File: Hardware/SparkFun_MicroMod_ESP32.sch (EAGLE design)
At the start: 45 parts, among them J1 MICROMOD-2222, Q2 MBT3904DW1T1, U1 W25QXX128MBIT-6X5, U2 ESP3212, U4 CP2102N, Y1 40MHZ, Y2 32.768kHz

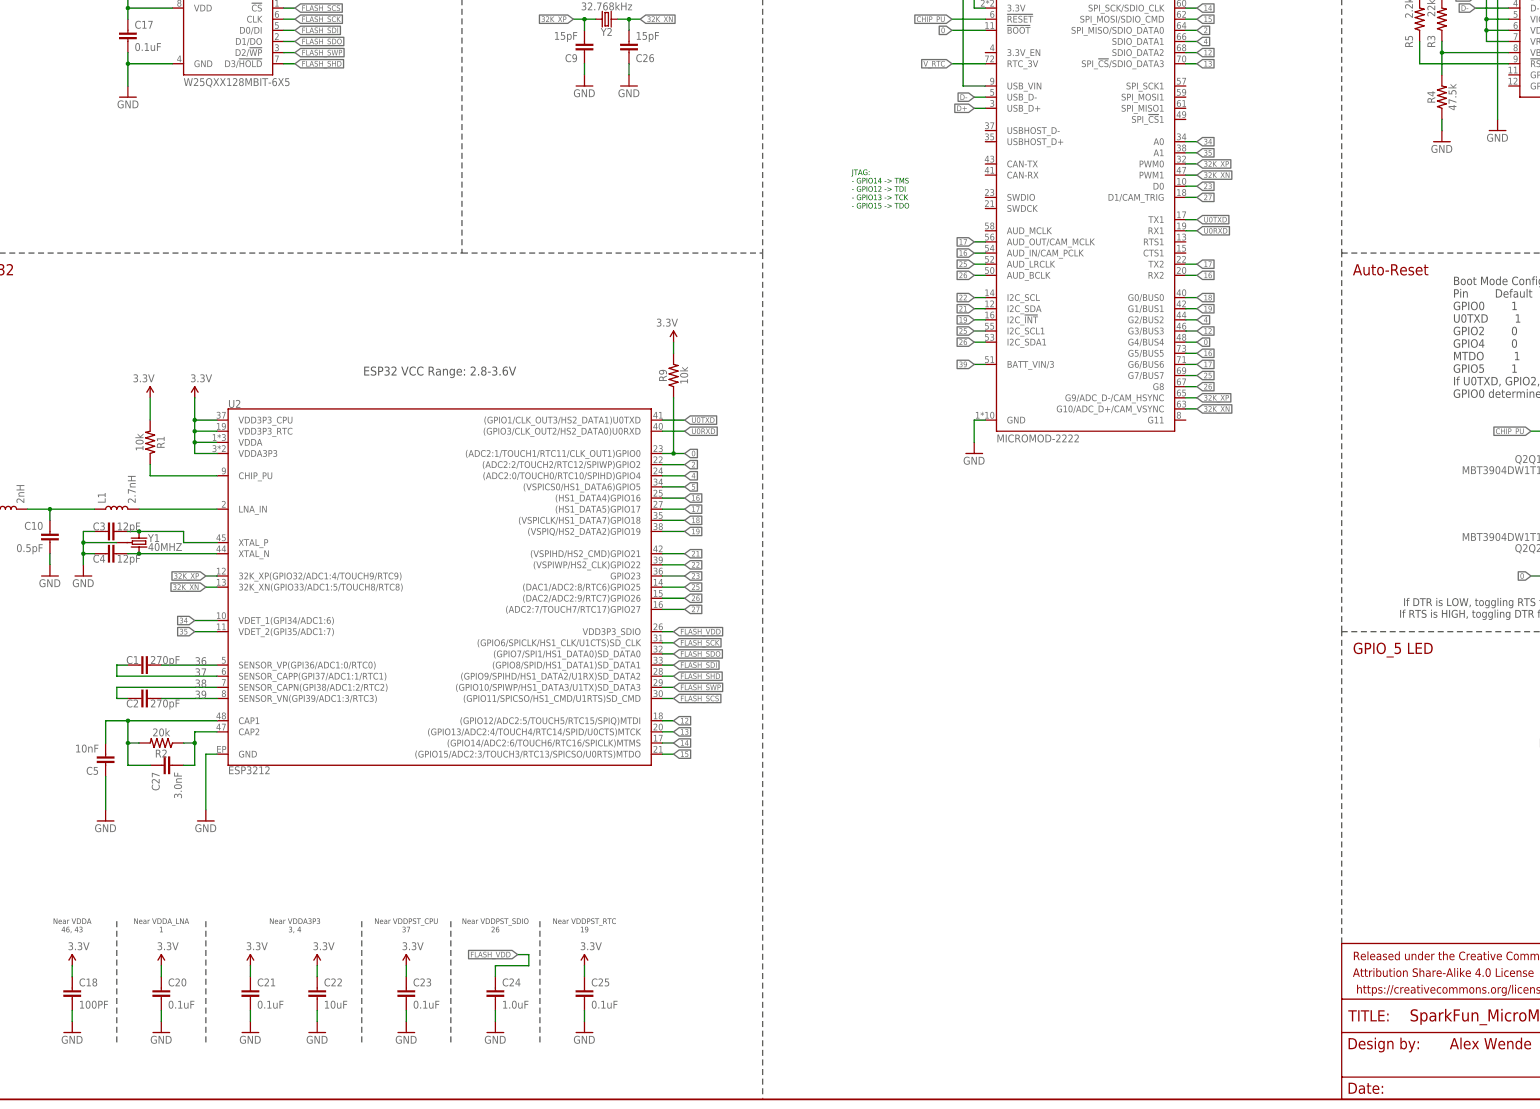
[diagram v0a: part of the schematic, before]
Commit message: updated Prod_IDs
Added missing PROD_IDs
Added Logos to sch
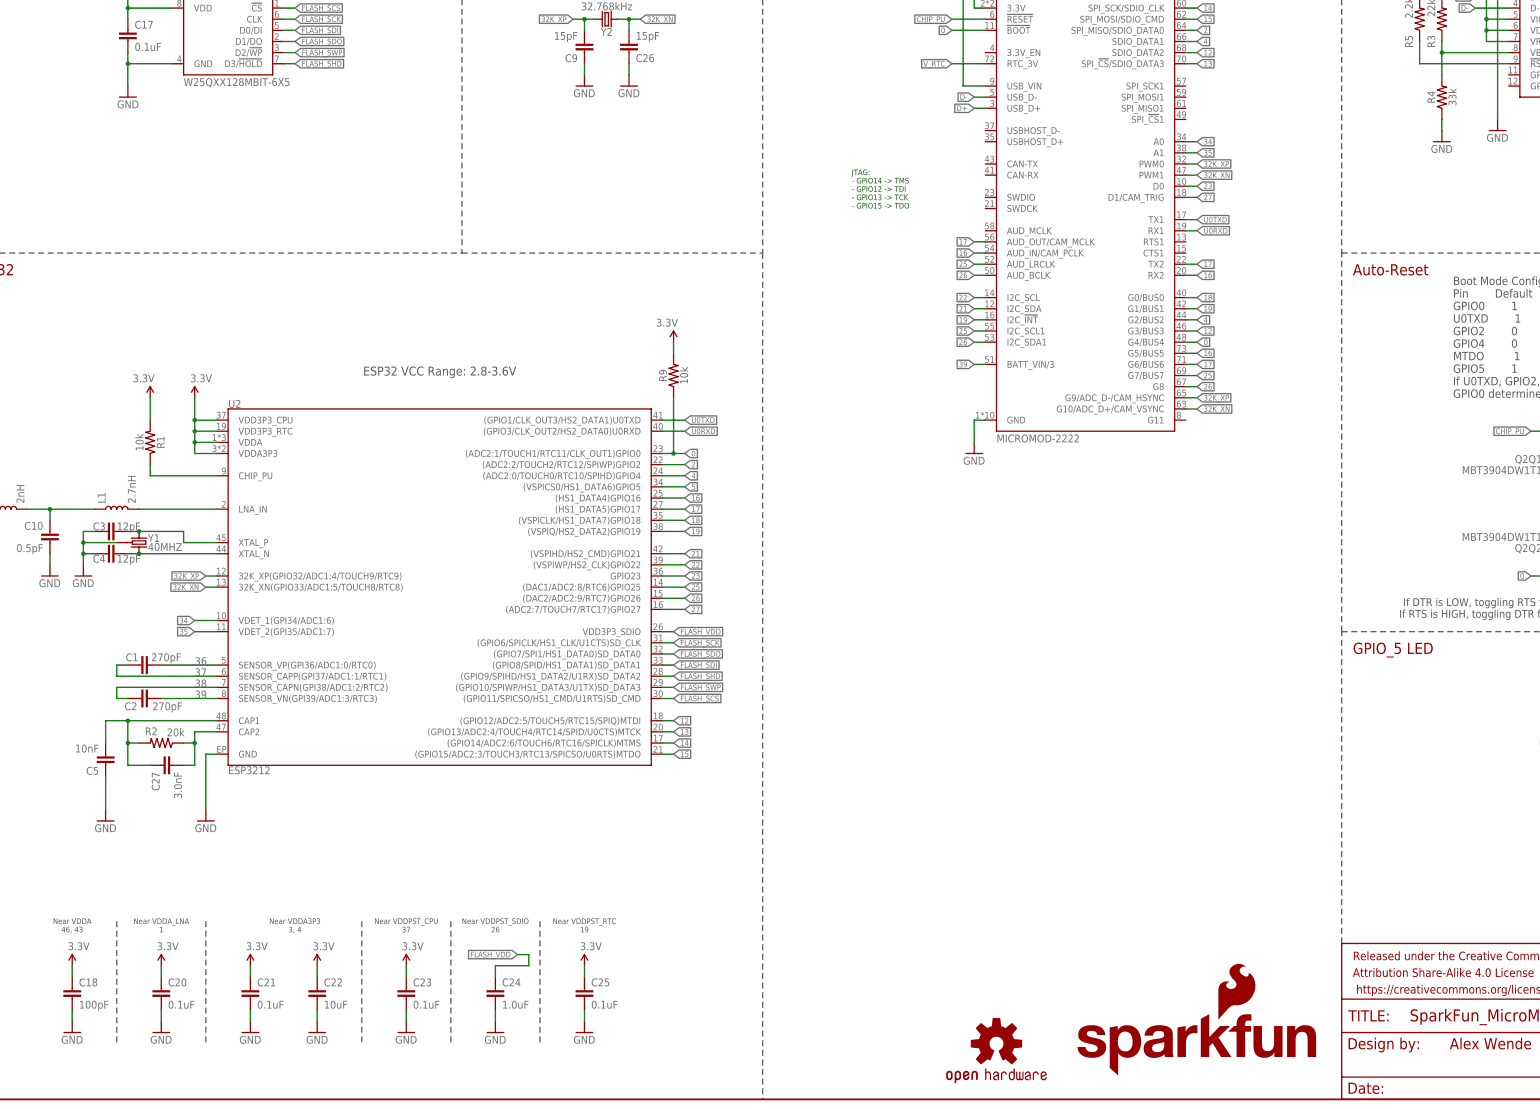
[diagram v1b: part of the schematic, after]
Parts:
- added LOGO2: SFE_LOGO_NAME_FLAME.1_INCH, SparkFun-Aesthetics:SFE_LOGO_NAME_FLAME.1_INCH
- added LOGO3: OSHW-LOGOS, SparkFun-Aesthetics:OSHW-LOGOS
- C1, C2: device SparkFun-Capacitors:4.7UF-0402_TIGHT-6.3V-20%-X5R -> SparkFun-Capacitors:270PF-0402T-50V-5%
- C10: device SparkFun-Capacitors:0.5PF-0402_TIGHT-20V-PM0.05PF-NP0 -> SparkFun-Capacitors:0.5PF-0402_TIGHT-50V-PM0.05PF-NP0
- C18: value 100PF -> 100pF; device SparkFun-Capacitors:CAP-0402-TIGHT -> SparkFun-Capacitors:100PF-0402T-50V-5%
- C27: device SparkFun-Capacitors:4.7UF-0402_TIGHT-6.3V-20%-X5R -> SparkFun-Capacitors:3.0NF-0402T-50V-5%
- R2: device SparkFun-Resistors:5.1KOHM-0402T-1/16W-1% -> SparkFun-Resistors:20KOHM-0402T-1/16W-1%
- R4: value 47.5k -> 33k; device SparkFun-Resistors:5.1KOHM-0402T-1/16W-1% -> SparkFun-Resistors:33KOHM-0402T-1/16W-1%
- Y1: device SparkFun-Clocks:CRYSTAL-40MHZ-SMD2-2X2.5MM -> SparkFun-Clocks:CRYSTAL-40MHZ-SMD-2X2.5MM
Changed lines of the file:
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@@
 <?xml version="1.0" encoding="utf-8"?>
 <!DOCTYPE eagle SYSTEM "eagle.dtd">
-<eagle version="9.6.0">
+<eagle version="9.4.1">
 <drawing>
 <settings>
-<setting alwaysvectorfont="yes"/>
+<setting alwaysvectorfont="no"/>
 <setting keepoldvectorfont="yes"/>
 <setting verticaltext="up"/>
@@
 <part name="SUPPLY2" library="SparkFun-Aesthetics" deviceset="3.3V" device=""/>
 <part name="GND2" library="SparkFun-Aesthetics" deviceset="GND" device=""/>
-<part name="Y1" library="SparkFun-Clocks" deviceset="CRYSTAL-40MHZ" device="-SMD2-2X2.5MM" value="40MHZ"/>
+<part name="Y1" library="SparkFun-Clocks" deviceset="CRYSTAL-40MHZ" device="-SMD-2X2.5MM" value="40MHZ"/>
 <part name="C3" library="SparkFun-Capacitors" deviceset="12PF" device="-0402T-50V-5%" value="12pF"/>
 <part name="C4" library="SparkFun-Capacitors" deviceset="12PF" device="-0402T-50V-5%" value="12pF"/>
-<part name="C1" library="SparkFun-Capacitors" deviceset="4.7UF" device="-0402_TIGHT-6.3V-20%-X5R" value="270pF"/>
-<part name="C2" library="SparkFun-Capacitors" deviceset="4.7UF" device="-0402_TIGHT-6.3V-20%-X5R" value="270pF"/>
+<part name="C1" library="SparkFun-Capacitors" deviceset="270PF" device="-0402T-50V-5%" value="270pF"/>
+<part name="C2" library="SparkFun-Capacitors" deviceset="270PF" device="-0402T-50V-5%" value="270pF"/>
 <part name="C5" library="SparkFun-Capacitors" deviceset="10NF" device="-0402T-25V-10%" value="10nF"/>
-<part name="R2" library="SparkFun-Resistors" deviceset="5.1KOHM" device="-0402T-1/16W-1%" value="20k"/>
+<part name="R2" library="SparkFun-Resistors" deviceset="20KOHM" device="-0402T-1/16W-1%" value="20k"/>
 <part name="GND3" library="SparkFun-Aesthetics" deviceset="GND" device=""/>
 <part name="GND36" library="SparkFun-Aesthetics" deviceset="GND" device=""/>
@@
 <part name="R17" library="SparkFun-Resistors" deviceset="10KOHM" device="-0402T-1/16W-1%" value="10k"/>
 <part name="R18" library="SparkFun-Resistors" deviceset="10KOHM" device="-0402T-1/16W-1%" value="10k"/>
-<part name="C18" library="SparkFun-Capacitors" deviceset="CAP" device="-0402-TIGHT" value="100PF"/>
+<part name="C18" library="SparkFun-Capacitors" deviceset="100PF" device="-0402T-50V-5%" value="100pF"/>
 <part name="SUPPLY9" library="SparkFun-Aesthetics" deviceset="3.3V" device=""/>
 <part name="GND5" library="SparkFun-Aesthetics" deviceset="GND" device=""/>
@@
 <part name="SUPPLY17" library="SparkFun-Aesthetics" deviceset="3.3V" device=""/>
 <part name="U2" library="esp32-thing-temp" deviceset="ESP3212" device=""/>
-<part name="C27" library="SparkFun-Capacitors" deviceset="4.7UF" device="-0402_TIGHT-6.3V-20%-X5R" value="3.0nF"/>
+<part name="C27" library="SparkFun-Capacitors" deviceset="3.0NF" device="-0402T-50V-5%" value="3.0nF"/>
 <part name="GND40" library="SparkFun-Aesthetics" deviceset="GND" device=""/>
 <part name="U4" library="SparkFun-IC-Comms" deviceset="CP2102N" device=""/>
@@
 <part name="SUPPLY8" library="SparkFun-Aesthetics" deviceset="3.3V" device=""/>
 <part name="R3" library="SparkFun-Resistors" deviceset="22KOHM" device="-0402_TIGHT-1/10W-1%" value="22k"/>
-<part name="R4" library="SparkFun-Resistors" deviceset="5.1KOHM" device="-0402T-1/16W-1%" value="47.5k"/>
+<part name="R4" library="SparkFun-Resistors" deviceset="33KOHM" device="-0402T-1/16W-1%" value="33k"/>
 <part name="GND11" library="SparkFun-Aesthetics" deviceset="GND" device=""/>
 <part name="SUPPLY14" library="SparkFun-Aesthetics" deviceset="V_USB" device=""/>
@@
 <part name="L1" library="SparkFun-Coils" deviceset="INDUCTOR" device="-0402_TIGHT-2.7NH" value="2.7nH"/>
 <part name="L2" library="SparkFun-Coils" deviceset="INDUCTOR" device="-0402_TIGHT-2.0NH" value="2nH"/>
-<part name="C10" library="SparkFun-Capacitors" deviceset="0.5PF" device="-0402_TIGHT-20V-PM0.05PF-NP0" value="0.5pF"/>
+<part name="C10" library="SparkFun-Capacitors" deviceset="0.5PF" device="-0402_TIGHT-50V-PM0.05PF-NP0" value="0.5pF"/>
 <part name="GND12" library="SparkFun-Aesthetics" deviceset="GND" device=""/>
 <part name="FD1" library="SparkFun-Aesthetics" deviceset="FIDUCIAL" device="UFIDUCIAL" value="FIDUCIALUFIDUCIAL"/>
@@
 <part name="FD4" library="SparkFun-Aesthetics" deviceset="FIDUCIAL" device="UFIDUCIAL" value="FIDUCIALUFIDUCIAL"/>
 <part name="LOGO1" library="SparkFun-Aesthetics" deviceset="SPECIAL_INSTRUCTIONS" device="-ORDERING"/>
+<part name="LOGO2" library="SparkFun-Aesthetics" deviceset="SFE_LOGO_NAME_FLAME" device=".1_INCH"/>
+<part name="LOGO3" library="SparkFun-Aesthetics" deviceset="OSHW-LOGO" device="S"/>
 </parts>
 <sheets>
@@
 </instance>
 <instance part="C1" gate="G$1" x="58.42" y="99.06" smashed="yes" rot="R90">
-<attribute name="NAME" x="55.88" y="99.314" size="1.778" layer="95" rot="MR0"/>
-<attribute name="VALUE" x="58.42" y="99.314" size="1.778" layer="96"/>
+<attribute name="NAME" x="52.832" y="99.949" size="1.778" layer="95" font="vector"/>
+<attribute name="VALUE" x="58.674" y="99.949" size="1.778" layer="96" font="vector"/>
 </instance>
 <instance part="C2" gate="G$1" x="58.42" y="91.44" smashed="yes" rot="MR270">
-<attribute name="NAME" x="55.88" y="91.186" size="1.778" layer="95" align="top-right"/>
-<attribute name="VALUE" x="58.42" y="91.186" size="1.778" layer="96" rot="MR180"/>
+<attribute name="NAME" x="52.578" y="90.551" size="1.778" layer="95" font="vector" rot="MR180"/>
+<attribute name="VALUE" x="58.928" y="90.551" size="1.778" layer="96" font="vector" rot="MR180"/>
 </instance>
 <instance part="C5" gate="G$1" x="48.26" y="78.74" smashed="yes" rot="R180">
@@
 <attribute name="VALUE" x="46.736" y="80.899" size="1.778" layer="96" font="vector" rot="R180"/>
 </instance>
-<instance part="R2" gate="R1" x="60.96" y="81.28" smashed="yes" rot="R180">
-<attribute name="NAME" x="60.96" y="79.756" size="1.778" layer="95" font="vector" rot="R180" align="bottom-center"/>
-<attribute name="VALUE" x="60.96" y="82.804" size="1.778" layer="96" font="vector" rot="R180" align="top-center"/>
+<instance part="R2" gate="G$1" x="60.96" y="81.28" smashed="yes" rot="R180">
+<attribute name="NAME" x="58.674" y="83.058" size="1.778" layer="95" font="vector" align="bottom-center"/>
+<attribute name="VALUE" x="64.262" y="82.804" size="1.778" layer="96" font="vector" rot="R180" align="top-center"/>
 </instance>
 <instance part="GND3" gate="1" x="48.26" y="63.5" smashed="yes">
@@
 <attribute name="VALUE" x="351.536" y="248.92" size="1.778" layer="96" font="vector" rot="R270" align="top-center"/>
 </instance>
-<instance part="R4" gate="R1" x="353.06" y="228.6" smashed="yes" rot="R90">
+<instance part="R4" gate="G$1" x="353.06" y="228.6" smashed="yes" rot="R90">
 <attribute name="NAME" x="351.536" y="228.6" size="1.778" layer="95" font="vector" rot="R90" align="bottom-center"/>
 <attribute name="VALUE" x="354.584" y="228.6" size="1.778" layer="96" font="vector" rot="R90" align="top-center"/>
@@
 <instance part="FD4" gate="G$1" x="424.18" y="17.78" smashed="yes"/>
 <instance part="LOGO1" gate="G$1" x="408.94" y="33.02" smashed="yes"/>
+<instance part="LOGO2" gate="G$1" x="269.24" y="5.08" smashed="yes"/>
+<instance part="LOGO3" gate="G$1" x="251.46" y="12.7" smashed="yes"/>
 </instances>
 <busses>
@@
 </segment>
 <segment>
-<pinref part="R4" gate="R1" pin="1"/>
+<pinref part="R4" gate="G$1" pin="1"/>
 <wire x1="353.06" y1="223.52" x2="353.06" y2="220.98" width="0.1524" layer="91"/>
 <pinref part="GND11" gate="1" pin="GND"/>
@@
 <wire x1="53.34" y1="76.2" x2="53.34" y2="81.28" width="0.1524" layer="91"/>
 <junction x="53.34" y="86.36"/>
-<pinref part="R2" gate="R1" pin="2"/>
+<pinref part="R2" gate="G$1" pin="2"/>
 <wire x1="53.34" y1="81.28" x2="53.34" y2="86.36" width="0.1524" layer="91"/>
 <wire x1="55.88" y1="81.28" x2="53.34" y2="81.28" width="0.1524" layer="91"/>
@@
 <wire x1="68.58" y1="81.28" x2="68.58" y2="83.82" width="0.1524" layer="91"/>
 <wire x1="68.58" y1="83.82" x2="73.66" y2="83.82" width="0.1524" layer="91"/>
-<pinref part="R2" gate="R1" pin="1"/>
+<pinref part="R2" gate="G$1" pin="1"/>
 <wire x1="66.04" y1="81.28" x2="68.58" y2="81.28" width="0.1524" layer="91"/>
 <junction x="68.58" y="81.28"/>
@@
 <pinref part="R3" gate="G$1" pin="1"/>
 <wire x1="353.06" y1="238.76" x2="353.06" y2="241.3" width="0.1524" layer="91"/>
-<pinref part="R4" gate="R1" pin="2"/>
+<pinref part="R4" gate="G$1" pin="2"/>
 <wire x1="353.06" y1="233.68" x2="353.06" y2="238.76" width="0.1524" layer="91"/>
 <junction x="353.06" y="238.76"/>

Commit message: Updated design
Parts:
- removed L2: 2nH, SparkFun-Coils:INDUCTOR-0402_TIGHT-2.0NH
- added C8: (no value), SparkFun-Capacitors:CAP-0402-TIGHT
- added TP1, TP2: TEST-POINT3, SparkFun-Connectors:TEST-POINT3
- A1: value ANTENNA-2.4GHZ-3.2X1.6MM-REDUCED -> ANTENNA2.4GHZ-8.0X1.0MM; device SparkFun-RF:ANTENNA-2.4GHZ-3.2X1.6MM-REDUCED -> SparkFun-RF:ANTENNA2.4GHZ-8.0X1.0MM
- C10: value 0.5pF -> (none); device SparkFun-Capacitors:0.5PF-0402_TIGHT-50V-PM0.05PF-NP0 -> SparkFun-Capacitors:CAP-0402-TIGHT
- Q2: device esp32-thing-temp:MBT3904DW1T1 -> SparkFun-DiscreteSemi:TRANS_NPN_DUAL-MBT3904DW1T1
- U2: value ESP3212 -> ESP32; device esp32-thing-temp:ESP3212 -> SparkFun-RF:ESP32
- Y1: value 40MHZ -> 40MHz
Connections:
- net 13 renamed 13-SPI_!CS!/SD_DATA3
- net 14 renamed 14-SPI_SCK/SD_CLK
- net 15 renamed 15-SPI_MOSI/SD_CMD
- net 2 renamed 2-SPI_MISO/SD_DATA0
- net 21 renamed 21-SDA
- net 22 renamed 22-SCL
- net 23 renamed 23-D0
- net 27 renamed 27-D1
- net 34 renamed 34-A0
- net 35 renamed 35-A1
- net 39 renamed 39-BATT/3
- net 5 renamed 5-STAT_LED
- net CHIP_PU renamed !RESET
- net FLASH_SCK renamed FLASH_SD_CLK
- net FLASH_SCS renamed FLASH_SD_CMD
- net FLASH_SDI renamed FLASH_SD_DATA1
- net FLASH_SDO renamed FLASH_SD_DATA0
- net FLASH_SHD renamed FLASH_SD_DATA2
- net FLASH_SWP renamed FLASH_SD_DATA3
- removed net 0: J1.!BOOT!, J1.G4/BUS4, Q2Q2.C, R9.1, U2.(ADC2:1/TOUCH1/RTC11/CLK_OUT1)GPIO0
- removed net 12: J1.G3/BUS3, J1.SDIO_DATA2, U2.(GPIO12/ADC2:5/TOUCH5/RTC15/SPIQ)MTDI
- removed net 16: J1.AUD_IN/CAM_PCLK, J1.G5/BUS5, J1.RX2, U2.(HS1_DATA4)GPIO16
- removed net 17: J1.AUD_OUT/CAM_MCLK, J1.G6/BUS6, J1.TX2, U2.(HS1_DATA5)GPIO17
- removed net 18: J1.G0/BUS0, U2.(VSPICLK/HS1_DATA7)GPIO18
- removed net 19: J1.G1/BUS1, J1.I2C_!INT!, U2.(VSPIQ/HS2_DATA2)GPIO19
- removed net 25: J1.AUD_LRCLK, J1.G7/BUS7, J1.I2C_SCL1, U2.(DAC1/ADC2:8/RTC6)GPIO25
- removed net 26: J1.AUD_BCLK, J1.G8, J1.I2C_SDA1, U2.(DAC2/ADC2:9/RTC7)GPIO26
- removed net 32K_XN: C26.2, J1.G10/ADC_D+/CAM_VSYNC, J1.PWM1, U2.32K_XN(GPIO33/ADC1:5/TOUCH8/RTC8), Y2.2
- removed net 32K_XP: C9.2, J1.G9/ADC_D-/CAM_HSYNC, J1.PWM0, U2.32K_XP(GPIO32/ADC1:4/TOUCH9/RTC9), Y2.1
- removed net 4: J1.G2/BUS2, J1.SDIO_DATA1, U2.(ADC2:0/TOUCH0/RTC10/SPIHD)GPIO4
- removed net N$6: C10.1, L1.1, L2.2
- removed net V_RTC: J1.RTC_3V
- new net 0-!BOOT!/I2C_!INT: J1.!BOOT!, J1.I2C_!INT!, Q2Q2.C, R9.1, U2.(ADC2:1/TOUCH1/RTC11/CLK_OUT1)GPIO0
- new net 12-SD_DATA2/G1: J1.G1/BUS1, J1.SDIO_DATA2, U2.(GPIO12/ADC2:5/TOUCH5/RTC15/SPIQ)MTDI
- new net 16-G2/RX1/AUD_IN: J1.AUD_IN/CAM_PCLK, J1.G2/BUS2, J1.RX1, U2.(HS1_DATA4)GPIO16
- new net 17-G3/TX1/AUD_OUT: J1.AUD_OUT/CAM_MCLK, J1.G3/BUS3, J1.TX1, U2.(HS1_DATA5)GPIO17
- new net 18-PWM0: J1.PWM0, U2.(VSPICLK/HS1_DATA7)GPIO18
- new net 19-PWM1: J1.PWM1, U2.(VSPIQ/HS2_DATA2)GPIO19
- new net 25-G4/AUD_LRCLK/SCL1: J1.AUD_LRCLK, J1.G4/BUS4, J1.I2C_SCL1, U2.(DAC1/ADC2:8/RTC6)GPIO25
- new net 26-G5/AUD_BCLK/SDA1: J1.AUD_BCLK, J1.G5/BUS5, J1.I2C_SDA1, U2.(DAC2/ADC2:9/RTC7)GPIO26
- new net 32-G6/RTC: C9.2, J1.G6/BUS6, U2.32K_XP(GPIO32/ADC1:4/TOUCH9/RTC9), Y2.1
- new net 33-G7/RTC: C26.2, J1.G7/BUS7, U2.32K_XN(GPIO33/ADC1:5/TOUCH8/RTC8), Y2.2
- new net 4-SD_DATA1/G0: J1.G0/BUS0, J1.SDIO_DATA1, U2.(ADC2:0/TOUCH0/RTC10/SPIHD)GPIO4
- net GND: now also C8.2
- net N$5: now also C8.1, L1.1; no longer L2.1
- net N$8: now also C10.1
- net U0RXD: now also TP1.1; no longer J1.RX1
- net U0TXD: now also TP2.1; no longer J1.TX1
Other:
- note added: "Status LED"
- note added: "v01"
- note removed: "GPIO_5 LED"
- note removed: "v10"
- moved on the sheet: A1, C1, C10, C17, C2, C26, C27, C3, C4, C5, C9, L1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
